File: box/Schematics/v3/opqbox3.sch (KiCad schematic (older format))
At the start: 2 parts, among them J1 Conn_01x02_Male, J2 Conn_01x02_Male

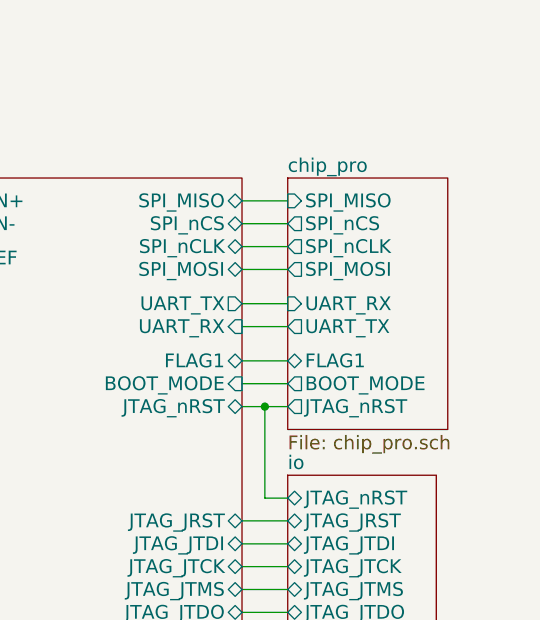
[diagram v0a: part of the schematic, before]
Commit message: remove chip, replace pi
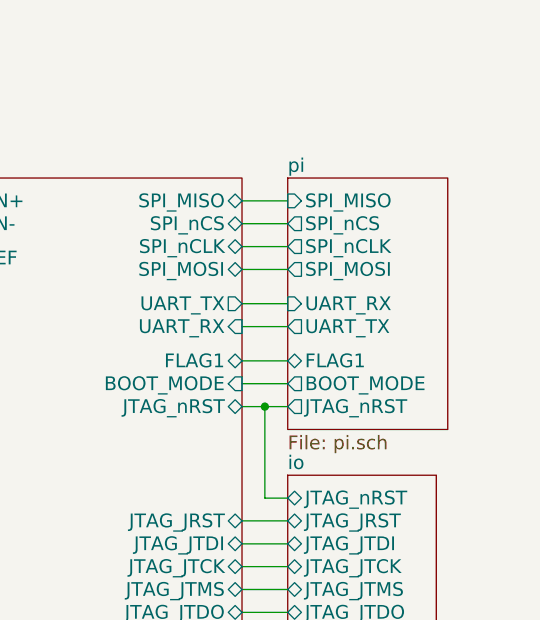
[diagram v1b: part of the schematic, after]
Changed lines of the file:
@@
 S 4950 1200 700  1100
 U 5A9ABA19
-F0 "chip_pro" 60
-F1 "chip_pro.sch" 60
+F0 "pi" 60
+F1 "pi.sch" 60
 F2 "SPI_MOSI" O L 4950 1600 60
 F3 "SPI_MISO" I L 4950 1300 60

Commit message: Moved brokers to rust with mongo reporting
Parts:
- J1, J2: symbol Conn_01x02_Male -> opqbox3-rescue:Conn_01x02_Male
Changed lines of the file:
@@
-EESchema Schematic File Version 2
-LIBS:opqbox3
-LIBS:device
-LIBS:power
-LIBS:conn
+EESchema Schematic File Version 4
 LIBS:opqbox3-cache
-EELAYER 25 0
+EELAYER 26 0
 EELAYER END
 $Descr A4 11693 8268
@@
 $EndSheet
 $Comp
-L PWR_FLAG #FLG01
+L power:PWR_FLAG #FLG01
 U 1 1 5A82F319
 P 1900 1300
@@
 $EndComp
 $Comp
-L PWR_FLAG #FLG02
+L power:PWR_FLAG #FLG02
 U 1 1 5A82F35B
 P 1900 1700
@@
 	2700 500  2700 7750
 Wire Wire Line
-	1650 1350 2150 1350
-Wire Wire Line
-	1650 1750 2150 1750
+	1650 1350 1700 1350
+Wire Wire Line
+	1650 1750 1700 1750
 Wire Wire Line
 	1900 1700 1900 1750
@@
 NoConn ~ 3350 1850
 $Comp
-L Conn_01x02_Male J1
+L opqbox3-rescue:Conn_01x02_Male J1
 U 1 1 5A83BEC0
 P 1450 1250
@@
 $EndComp
 $Comp
-L Conn_01x02_Male J2
+L opqbox3-rescue:Conn_01x02_Male J2
 U 1 1 5A83C177
 P 1450 1650
@@
 	4750 2100 4950 2100
 Wire Wire Line
-	4750 2200 4950 2200
+	4750 2200 4850 2200
 Wire Wire Line
 	4750 3100 4950 3100
@@
 	4850 2600 4950 2600
 Connection ~ 4850 2200
+Wire Wire Line
+	1900 1750 2150 1750
+Wire Wire Line
+	1900 1350 2150 1350
+Wire Wire Line
+	1700 1350 1900 1350
+Wire Wire Line
+	1700 1750 1900 1750
+Wire Wire Line
+	4850 2200 4950 2200
 $EndSCHEMATC
